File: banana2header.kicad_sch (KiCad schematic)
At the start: 6 parts, among them J1 Conn_01x01_Female, J2 Conn_01x01_Female, J3 Conn_01x01_Female, J4 Molex_SL_01x03_Male, J5 Conn_01x02_Male, J6 Conn_01x02_Male

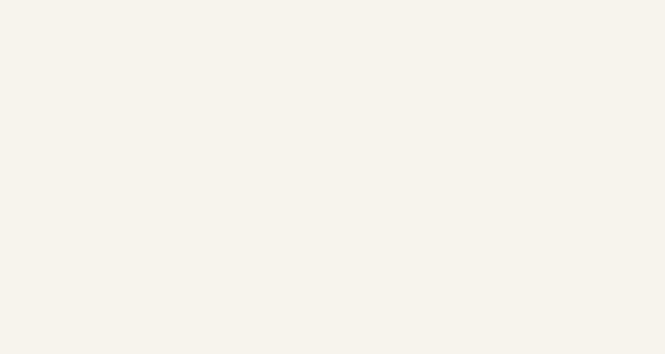
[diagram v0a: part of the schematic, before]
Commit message: add license decal
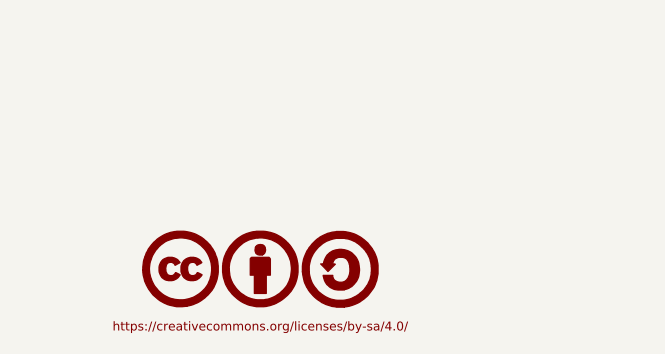
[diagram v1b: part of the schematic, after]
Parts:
- added LOGO1: CC-BY-SA_0.33in, Symbol_CreativeCommons:CC-BY-SA_SilkScreenTop_Small, symbol Creative_Commons:CC-BY-SA_0.33in
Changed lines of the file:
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@@
     (pin "1")
+  )
+  (symbol (lib_id "Creative_Commons:CC-BY-SA_0.33in") (at 153.67 180.34 0) (unit 1)
+    (in_bom yes) (on_board yes) (fields_autoplaced)
+    (property "Reference" "LOGO1" (id 0) (at 153.67 183.7944 0)
+      (effects (font (size 1.524 1.524)) hide)
+    )
+    (property "Value" "CC-BY-SA_0.33in" (id 1) (at 153.67 176.8856 0)
+      (effects (font (size 1.524 1.524)) hide)
+    )
+    (property "Footprint" "Symbol_CreativeCommons:CC-BY-SA_SilkScreenTop_Small" (id 2) (at 153.67 180.34 0)
+      (effects (font (size 1.27 1.27)) hide)
+    )
+    (property "Datasheet" "" (id 3) (at 153.67 180.34 0)
+      (effects (font (size 1.27 1.27)) hide)
+    )
   )
   (symbol (lib_id "Connector:Conn_01x01_Female") (at 149.86 77.47 0) (mirror y) (unit 1)
@@
       (reference "J6") (unit 1) (value "Conn_01x02_Male") (footprint "Connector_PinHeader_2.54mm:PinHeader_1x02_P2.54mm_Vertical")
     )
+    (path "/503c64e8-98a8-4b52-b5e7-484b5c98130a"
+      (reference "LOGO1") (unit 1) (value "CC-BY-SA_0.33in") (footprint "Symbol_CreativeCommons:CC-BY-SA_SilkScreenTop_Small")
+    )
   )
